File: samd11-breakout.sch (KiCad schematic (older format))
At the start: 17 parts, among them J1 USB_C_Receptacle, J2 DebugEdge_02x03, J3 Conn_01x10_Male, J4 Conn_01x10_Male, U1 USBLC6-2SC6, U2 MCP1700-3302E_SOT23, U3 SAMD11D14A-M

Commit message: save board outline
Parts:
- C1, C2: footprint Capacitor_SMD:C_0201_0603Metric -> Capacitor_SMD:C_0603_1608Metric
- D1: footprint LED_SMD:LED_0201_0603Metric -> LED_SMD:LED_0603_1608Metric
- R1, R2, R3, R4, R5, R6: footprint Resistor_SMD:R_0201_0603Metric -> Resistor_SMD:R_0603_1608Metric
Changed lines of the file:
@@
 F 0 "C2" H 5815 1446 50  0000 L CNN
 F 1 "1uF" H 5815 1355 50  0000 L CNN
-F 2 "Capacitor_SMD:C_0201_0603Metric" H 5738 1250 50  0001 C CNN
+F 2 "Capacitor_SMD:C_0603_1608Metric" H 5738 1250 50  0001 C CNN
 F 3 "~" H 5700 1400 50  0001 C CNN
 	1    5700 1400
@@
 F 0 "R2" V 4157 1950 50  0000 C CNN
 F 1 "5.1k" V 4066 1950 50  0000 C CNN
-F 2 "Resistor_SMD:R_0201_0603Metric" V 3880 1950 50  0001 C CNN
+F 2 "Resistor_SMD:R_0603_1608Metric" V 3880 1950 50  0001 C CNN
 F 3 "~" H 3950 1950 50  0001 C CNN
 	1    3950 1950
@@
 F 0 "R3" V 4150 2050 50  0000 C CNN
 F 1 "5.1k" V 4050 2050 50  0000 C CNN
-F 2 "Resistor_SMD:R_0201_0603Metric" V 3880 2050 50  0001 C CNN
+F 2 "Resistor_SMD:R_0603_1608Metric" V 3880 2050 50  0001 C CNN
 F 3 "~" H 3950 2050 50  0001 C CNN
 	1    3950 2050
@@
 F 0 "C1" H 4815 1446 50  0000 L CNN
 F 1 "1uF" H 4815 1355 50  0000 L CNN
-F 2 "Capacitor_SMD:C_0201_0603Metric" H 4738 1250 50  0001 C CNN
+F 2 "Capacitor_SMD:C_0603_1608Metric" H 4738 1250 50  0001 C CNN
 F 3 "~" H 4700 1400 50  0001 C CNN
 	1    4700 1400
@@
 F 0 "R1" H 2570 4846 50  0000 L CNN
 F 1 "1M" H 2570 4755 50  0000 L CNN
-F 2 "Resistor_SMD:R_0201_0603Metric" V 2430 4800 50  0001 C CNN
+F 2 "Resistor_SMD:R_0603_1608Metric" V 2430 4800 50  0001 C CNN
 F 3 "~" H 2500 4800 50  0001 C CNN
 	1    2500 4800
@@
 F 0 "R5" H 10170 2296 50  0000 L CNN
 F 1 "30k" H 10170 2205 50  0000 L CNN
-F 2 "Resistor_SMD:R_0201_0603Metric" V 10030 2250 50  0001 C CNN
+F 2 "Resistor_SMD:R_0603_1608Metric" V 10030 2250 50  0001 C CNN
 F 3 "~" H 10100 2250 50  0001 C CNN
 	1    10100 2250
@@
 F 0 "R6" H 10170 3196 50  0000 L CNN
 F 1 "47k" H 10170 3105 50  0000 L CNN
-F 2 "Resistor_SMD:R_0201_0603Metric" V 10030 3150 50  0001 C CNN
+F 2 "Resistor_SMD:R_0603_1608Metric" V 10030 3150 50  0001 C CNN
 F 3 "~" H 10100 3150 50  0001 C CNN
 	1    10100 3150
@@
 F 0 "D1" V 8589 1183 50  0000 R CNN
 F 1 "LED" V 8498 1183 50  0000 R CNN
-F 2 "LED_SMD:LED_0201_0603Metric" H 8550 1300 50  0001 C CNN
+F 2 "LED_SMD:LED_0603_1608Metric" H 8550 1300 50  0001 C CNN
 F 3 "~" H 8550 1300 50  0001 C CNN
 	1    8550 1300
@@
 F 0 "R4" H 8620 1846 50  0000 L CNN
 F 1 "1k" H 8620 1755 50  0000 L CNN
-F 2 "Resistor_SMD:R_0201_0603Metric" V 8480 1800 50  0001 C CNN
+F 2 "Resistor_SMD:R_0603_1608Metric" V 8480 1800 50  0001 C CNN
 F 3 "~" H 8550 1800 50  0001 C CNN
 	1    8550 1800

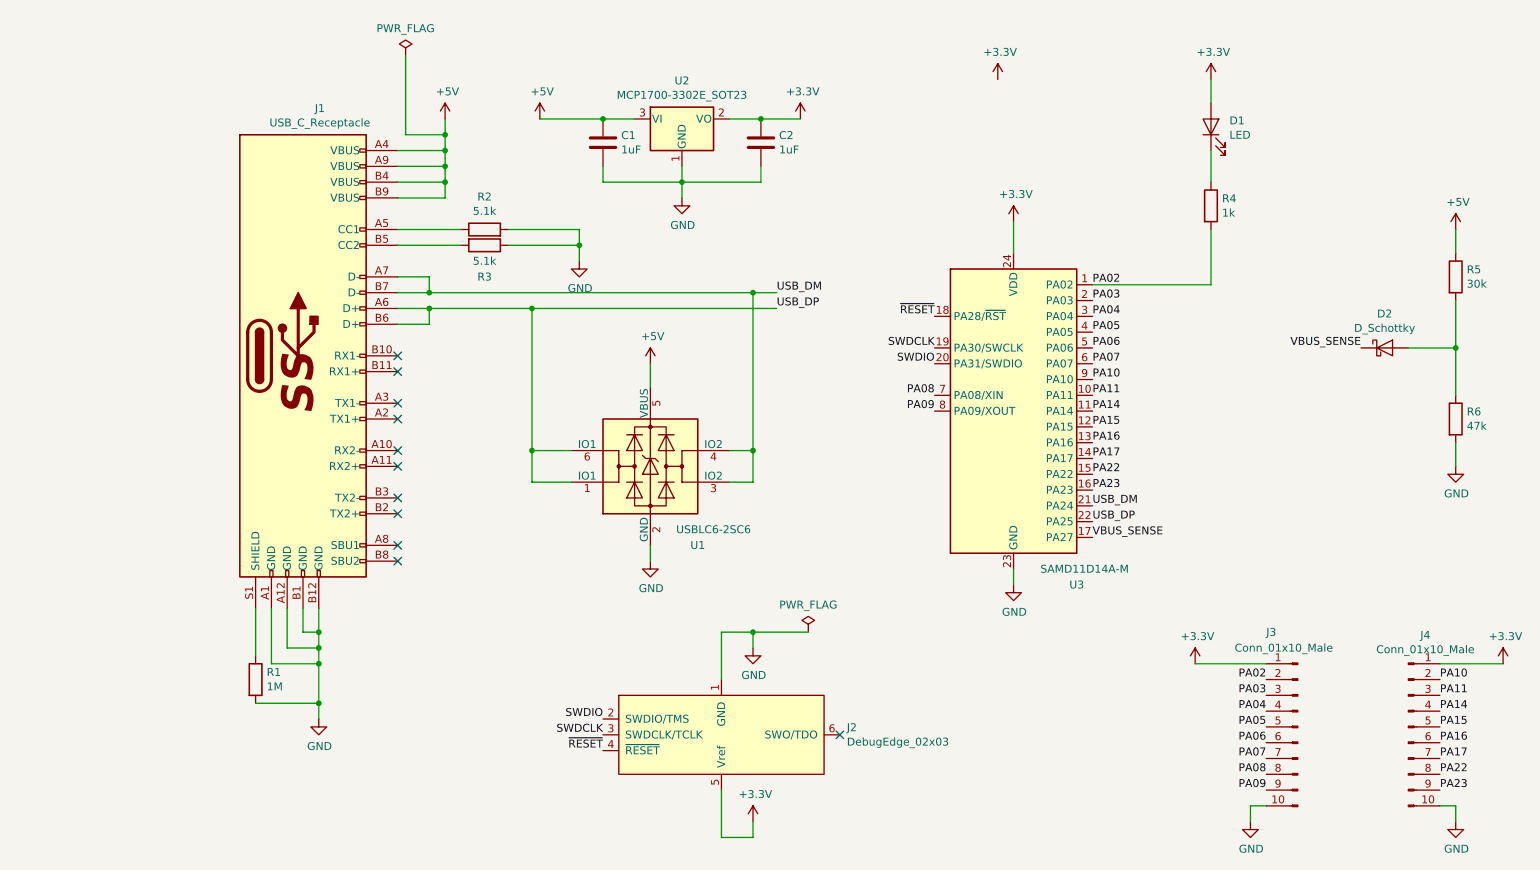
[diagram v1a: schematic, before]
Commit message: half routed
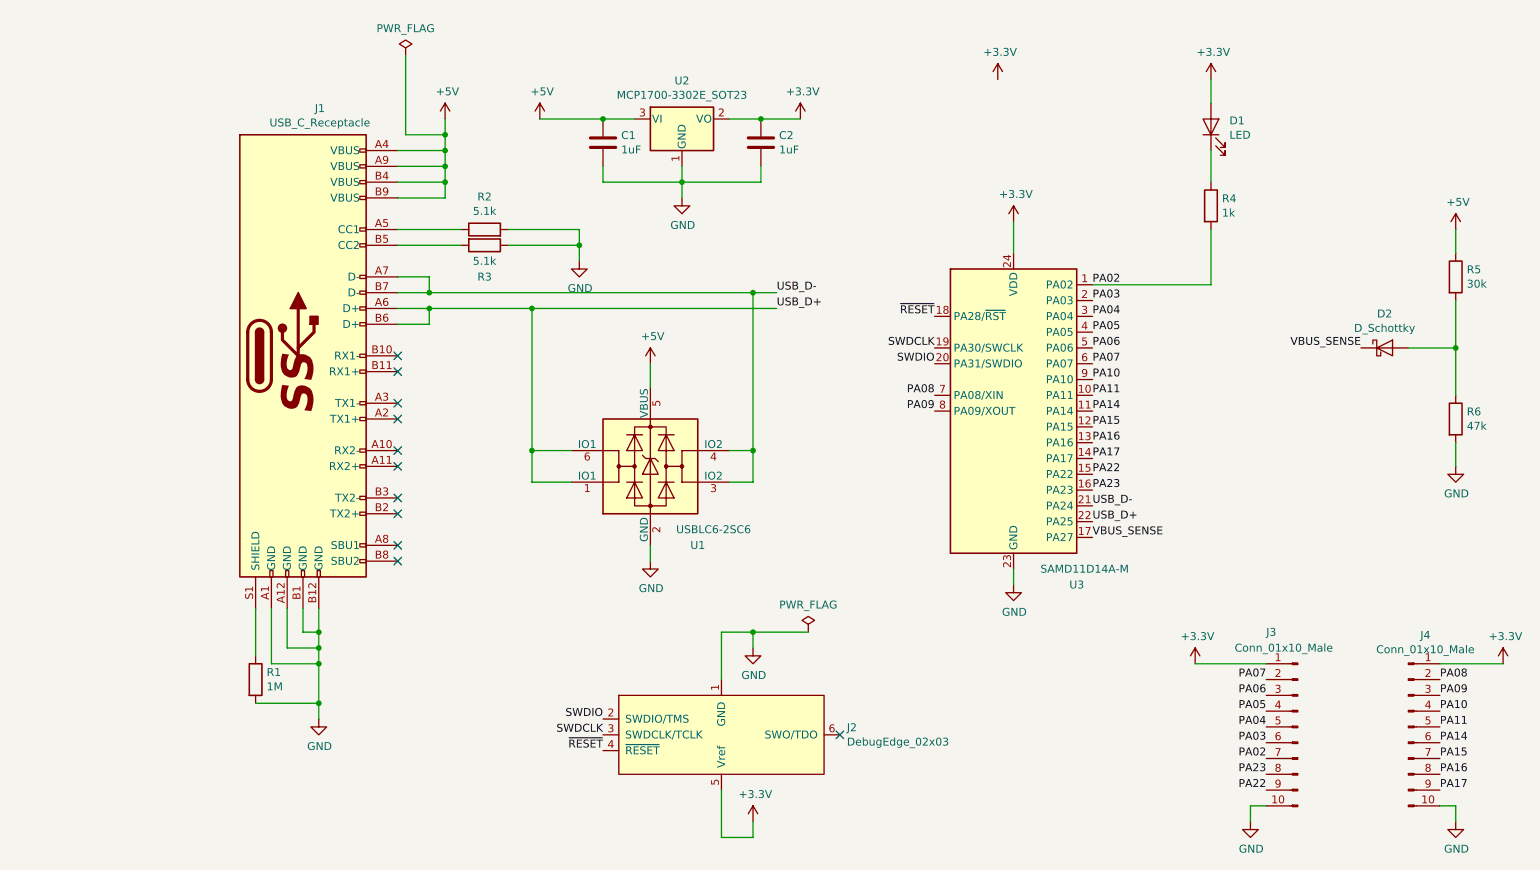
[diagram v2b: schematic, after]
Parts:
- J1: footprint project:USB_C_Receptacle_HRO_TYPE-C-31-M-12 -> project:USB_C_Receptacle_GCT_USB4085
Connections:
- net PA02: now also J3.7 (Pin_7); no longer J3.2 (Pin_2)
- net PA03: now also J3.6 (Pin_6); no longer J3.3 (Pin_3)
- net PA04: now also J3.5 (Pin_5); no longer J3.4 (Pin_4)
- net PA05: now also J3.4 (Pin_4); no longer J3.5 (Pin_5)
- net PA06: now also J3.3 (Pin_3); no longer J3.6 (Pin_6)
- net PA07: now also J3.2 (Pin_2); no longer J3.7 (Pin_7)
- net PA08: now also J4.2 (Pin_2); no longer J3.8 (Pin_8)
- net PA09: now also J4.3 (Pin_3); no longer J3.9 (Pin_9)
- net PA10: now also J4.4 (Pin_4); no longer J4.2 (Pin_2)
- net PA11: now also J4.5 (Pin_5); no longer J4.3 (Pin_3)
- net PA14: now also J4.6 (Pin_6); no longer J4.4 (Pin_4)
- net PA15: now also J4.7 (Pin_7); no longer J4.5 (Pin_5)
- net PA16: now also J4.8 (Pin_8); no longer J4.6 (Pin_6)
- net PA17: now also J4.9 (Pin_9); no longer J4.7 (Pin_7)
- net PA22: now also J3.9 (Pin_9); no longer J4.8 (Pin_8)
- net PA23: now also J3.8 (Pin_8); no longer J4.9 (Pin_9)
- net USB_DM renamed USB_D-
- net USB_DP renamed USB_D+
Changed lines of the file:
@@
 F 0 "J1" H 2907 4317 50  0000 C CNN
 F 1 "USB_C_Receptacle" H 2907 4226 50  0000 C CNN
-F 2 "project:USB_C_Receptacle_HRO_TYPE-C-31-M-12" H 2950 2750 50  0001 C CNN
+F 2 "project:USB_C_Receptacle_GCT_USB4085" H 2950 2750 50  0001 C CNN
 F 3 "http://www.usb.org/developers/docs/usb_31_033017.zip" H 2950 2750 50  0001 C CNN
 	1    2800 2750
@@
 $EndComp
 Text Label 7800 3700 0    50   ~ 0
-USB_DM
+USB_D-
 Text Label 7800 3800 0    50   ~ 0
-USB_DP
+USB_D+
 Text Label 5800 2350 0    50   ~ 0
-USB_DM
+USB_D-
 Text Label 5800 2450 0    50   ~ 0
-USB_DP
+USB_D+
 Wire Wire Line
 	3400 2450 3600 2450
@@
 Text Label 7800 3600 0    50   ~ 0
 PA23
+Text Label 8900 5300 2    50   ~ 0
+PA02
+Text Label 8900 5200 2    50   ~ 0
+PA03
+Text Label 8900 5100 2    50   ~ 0
+PA04
+Text Label 8900 5000 2    50   ~ 0
+PA05
+Text Label 8900 4900 2    50   ~ 0
+PA06
 Text Label 8900 4800 2    50   ~ 0
-PA02
-Text Label 8900 4900 2    50   ~ 0
-PA03
-Text Label 8900 5000 2    50   ~ 0
-PA04
-Text Label 8900 5100 2    50   ~ 0
-PA05
-Text Label 8900 5200 2    50   ~ 0
-PA06
-Text Label 8900 5300 2    50   ~ 0
 PA07
+Text Label 10000 4800 0    50   ~ 0
+PA08
+Text Label 10000 4900 0    50   ~ 0
+PA09
+Text Label 10000 5000 0    50   ~ 0
+PA10
+Text Label 10000 5100 0    50   ~ 0
+PA11
+Text Label 10000 5200 0    50   ~ 0
+PA14
+Text Label 10000 5300 0    50   ~ 0
+PA15
+Text Label 10000 5400 0    50   ~ 0
+PA16
+Text Label 10000 5500 0    50   ~ 0
+PA17
+Text Label 8900 5500 2    50   ~ 0
+PA22
 Text Label 8900 5400 2    50   ~ 0
-PA08
-Text Label 8900 5500 2    50   ~ 0
-PA09
-Text Label 10000 4800 0    50   ~ 0
-PA10
-Text Label 10000 4900 0    50   ~ 0
-PA11
-Text Label 10000 5000 0    50   ~ 0
-PA14
-Text Label 10000 5100 0    50   ~ 0
-PA15
-Text Label 10000 5200 0    50   ~ 0
-PA16
-Text Label 10000 5300 0    50   ~ 0
-PA17
-Text Label 10000 5400 0    50   ~ 0
-PA22
-Text Label 10000 5500 0    50   ~ 0
 PA23
 $Comp

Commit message: ok that should do it
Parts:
- removed J1: USB_C_Receptacle, project:USB_C_Receptacle_GCT_USB4085, symbol Connector:USB_C_Receptacle
- added J1: USB4105-GF-A, project:GCT_USB4105-GF-A, symbol USB4105-GF-A:USB4105-GF-A
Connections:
- net +5V: now also J1.A4_B9 (VBUS), J1.B4_A9 (VBUS)
- net GND: now also J1.A1_B12 (GND), J1.B1_A12 (GND)
- net PA23: now also J3.9 (Pin_9); no longer J3.8 (Pin_8)
- net USB_D+: now also J1.A6 (DP1), J1.B7 (DN2)
- net USB_D-: now also J1.A7 (DN1), J1.B6 (DP2)
- net VBUS_SENSE: now also U3.15 (PA22); no longer U3.17 (PA27)
- net CC2: now reaches R2.1
- net CC2: now also J1.B5 (CC2)
- net CC1: now reaches R3.2
- net CC1: now also J1.A5 (CC1)
- net USB_SHIELD: now reaches R1.1
- net USB_SHIELD: now also J1.A8 (SBU1), J1.B8 (SBU2), J1.S1 (SHELL_GND), J1.S2 (SHELL_GND), J1.S3 (SHELL_GND), J1.S4 (SHELL_GND)
- removed net PA22: J3.9 (Pin_9), U3.15 (PA22)
- new net PA27: J3.8 (Pin_8), U3.17 (PA27)
- no-connect marks 11 -> 1
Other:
- moved on the sheet: R1, R2
